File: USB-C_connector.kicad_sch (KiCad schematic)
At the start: 14 parts, among them J2 USB_C_Receptacle_USB2.0_14P, U5 TPS62A01ADRL

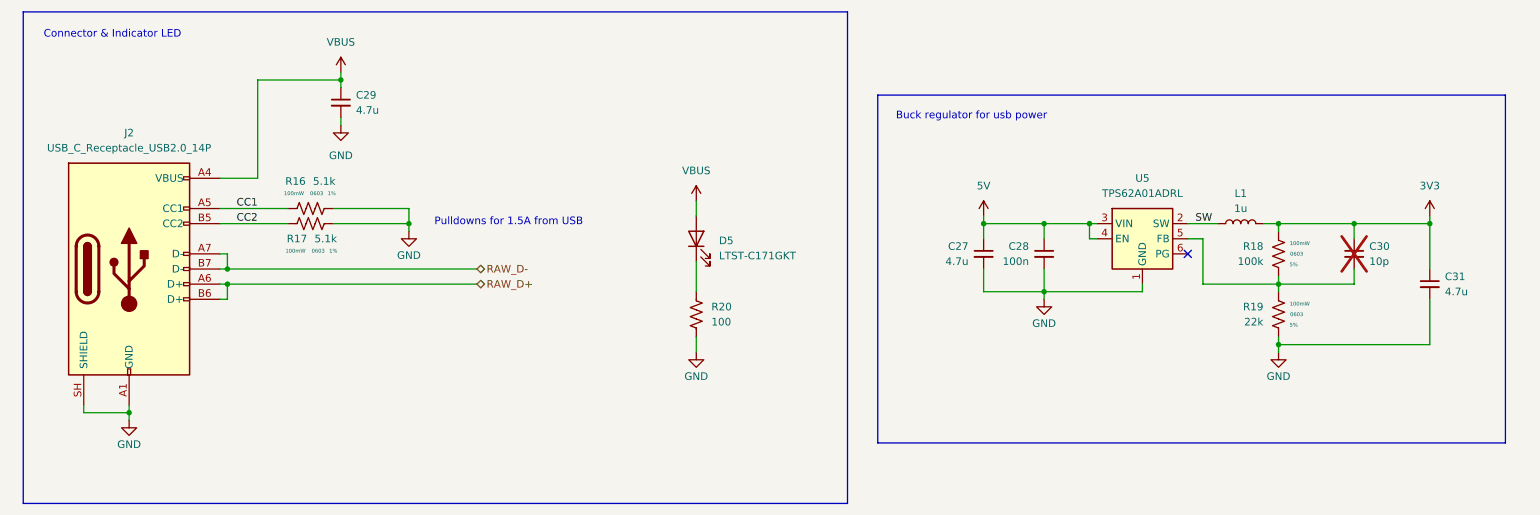
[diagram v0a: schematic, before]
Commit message: Finished schematic, added power section for external power (both power supply and battery), added current sensing for TX microcontroller
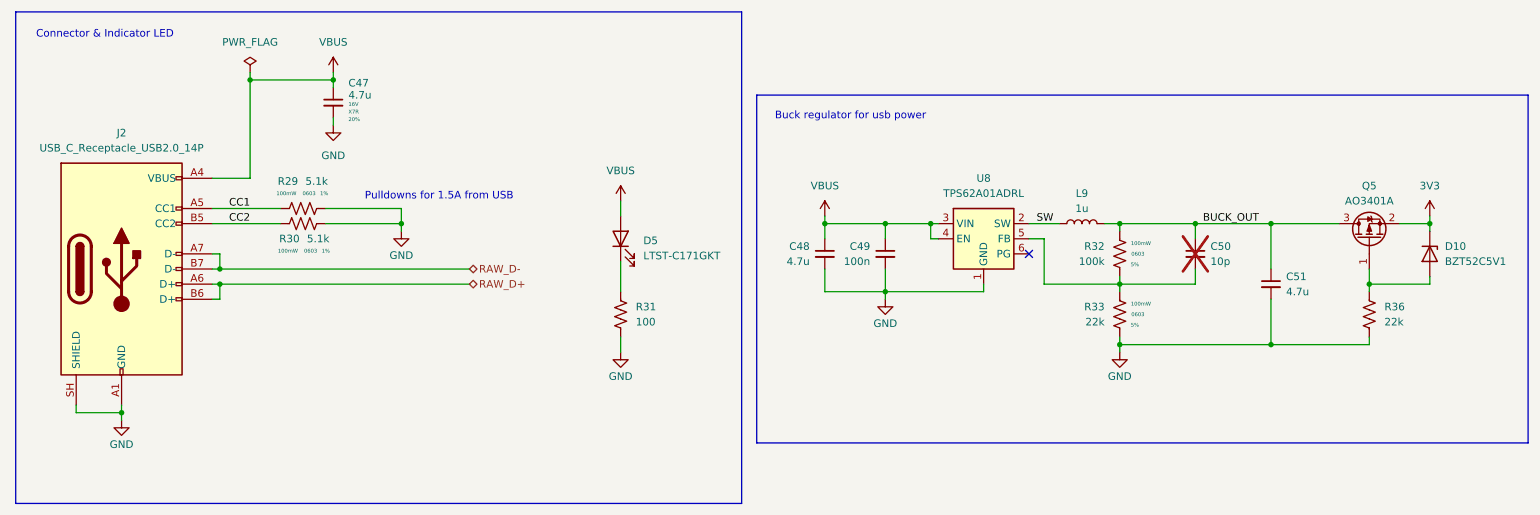
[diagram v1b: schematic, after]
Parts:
- removed C29: 4.7u, Capacitor_SMD:C_0603_1608Metric, symbol Device:C_Small
- added C47: 4.7u, Capacitor_SMD:C_0603_1608Metric_Pad1.08x0.95mm_HandSolder, symbol AERO_Capacitors:C_0603
- added D10: BZT52C5V1, Diode_SMD:D_SOD-123, symbol Device:D_Zener
- added Q5: AO3401A, Package_TO_SOT_SMD:SOT-23, symbol Transistor_FET:AO3401A
- added R36: 22k, Resistor_SMD:R_0603_1608Metric_Pad0.98x0.95mm_HandSolder, symbol Device:R_US
- renumbered C27 to C48, C28 to C49, C30 to C50, C31 to C51, L1 to L9, R16 to R29, R17 to R30, R20 to R31, R18 to R32, R19 to R33, U5 to U8
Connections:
- net 5V is gone; now on net VBUS: C48.1, C49.1, U8.3 (VIN), U8.4 (EN)
- net 3V3: now also D10.1 (K), Q5.2 (S); no longer C50.1, C51.1, L9.2, R32.2
- net GND: now also C47.2, R36.2
- net VBUS: now also C47.1
- new net: D10.2 (A), Q5.1 (G), R36.1
- new net BUCK_OUT: C50.1, C51.1, L9.2, Q5.3 (D), R32.2
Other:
- moved on the sheet: C48, C49, C50, C51, D5, J2, L9, R29, R30, R31, R32, R33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

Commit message: Made most capacitors 0402 for mcu sheets, defined board shape and started layout
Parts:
- removed C48: 4.7u, Capacitor_SMD:C_0603_1608Metric, symbol Device:C_Small
- removed C49: 100n, Capacitor_SMD:C_0603_1608Metric, symbol Device:C_Small
- removed R31: 100, Resistor_SMD:R_0603_1608Metric_Pad0.98x0.95mm_HandSolder, symbol Device:R_US
- removed R36: 22k, Resistor_SMD:R_0603_1608Metric_Pad0.98x0.95mm_HandSolder, symbol Device:R_US
- added C50: 4.7u, Capacitor_SMD:C_0603_1608Metric_Pad1.08x0.95mm_HandSolder, symbol AERO_Capacitors:C_0603
- added C51: 100n, Capacitor_SMD:C_0603_1608Metric_Pad1.08x0.95mm_HandSolder, symbol AERO_Capacitors:C_0603
- added R32: 100, Resistor_SMD:R_0603_1608Metric_Pad0.98x0.95mm_HandSolder, symbol AERO_Resistors:R_0603
- added R35: 22k, Resistor_SMD:R_0603_1608Metric_Pad0.98x0.95mm_HandSolder, symbol AERO_Resistors:R_0603
- renumbered C47 to C49, C50 to C52, C51 to C53, D10 to D6, J2 to J3, R29 to R30, R30 to R31, R32 to R33, R33 to R34
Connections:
- net GND: now also C50.2, C51.2, R32.1, R35.1
- net VBUS: now also C50.1, C51.1
- net at D6.2 (A), Q5.1 (G): now also R35.2
- net at D5.1 (K): now also R32.2
